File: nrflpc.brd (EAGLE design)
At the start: 67.9 x 38.8 mm, 75 parts, among them IC1 LPC1111/12/13/14-HVQFN33, IC2 LT1763CS8-3.3, IC3 LM3401, IC5 LM3401, IC6 LM3401, IC7 LM3401, Q1 20MHz, Q2 MOSFET-PCHANNEL, Q3 MOSFET-PCHANNEL, Q4 MOSFET-PCHANNEL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

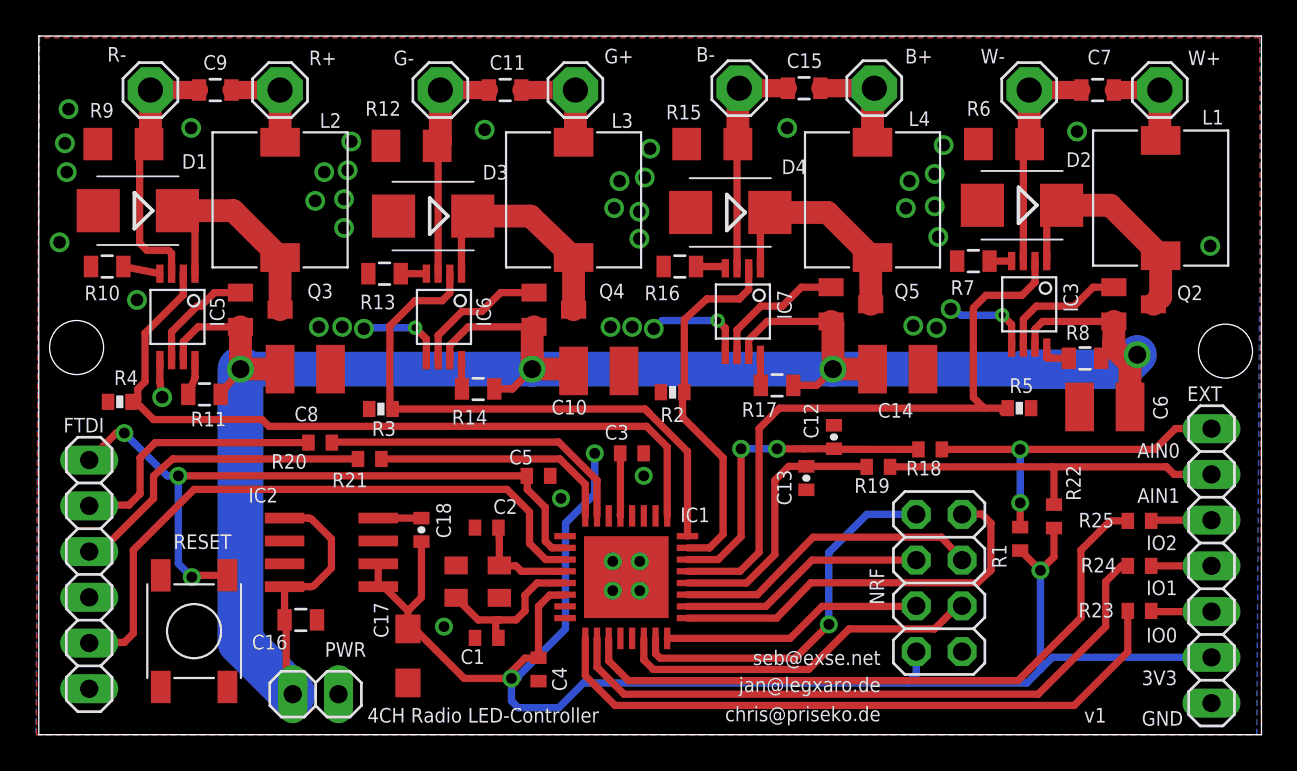
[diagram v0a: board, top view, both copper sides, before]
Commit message: More silkscreen
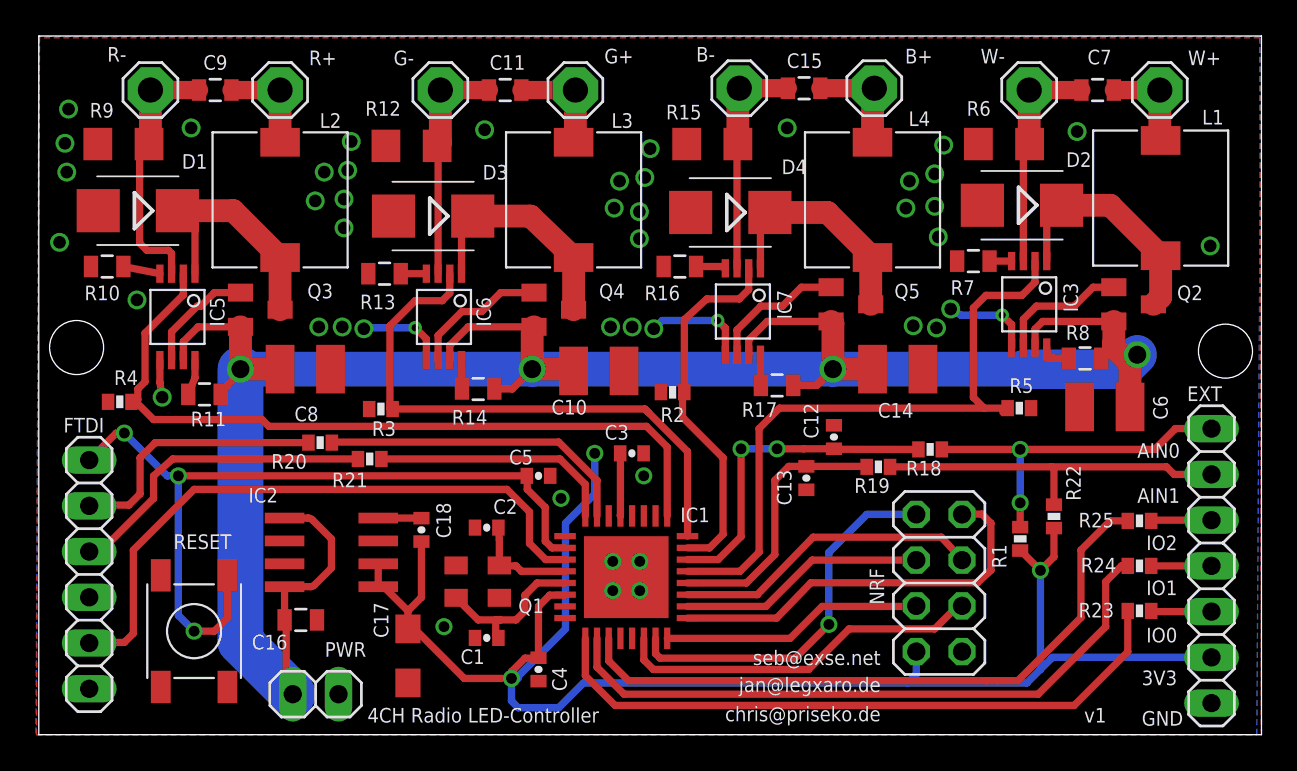
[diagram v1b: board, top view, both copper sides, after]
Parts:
- C1, C2, C3, C4, C5: device rcl:C0402 -> SparkFun-Passives:0402-CAP
- C12, C13: device SparkFun:0402-CAP -> SparkFun-Passives:0402-CAP
- R1, R18, R19, R20, R21, R22, R23, R24, R25: device rcl:R0402 -> SparkFun-Resistors:0402-RES
- R2, R3, R4, R5: device SparkFun:0402-RES -> SparkFun-Resistors:0402-RES
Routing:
- net !RST: track 39.2 -> 44.7 mm
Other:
- board text added: "Q1"

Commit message: Silkscreen
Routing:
- net GND: vias 48 -> 60
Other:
- board text added: "<<</>>"
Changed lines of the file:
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@@
 <grid distance="0.125" unitdist="mm" unit="mm" style="dots" multiple="1" display="yes" altdistance="0.03125" altunitdist="mm" altunit="mm"/>
 <layers>
-<layer number="1" name="Top" color="4" fill="1" visible="yes" active="yes"/>
+<layer number="1" name="Top" color="4" fill="1" visible="no" active="yes"/>
 <layer number="2" name="Route2" color="1" fill="3" visible="no" active="no"/>
 <layer number="3" name="Route3" color="4" fill="3" visible="no" active="no"/>
@@
 <layer number="14" name="Route14" color="1" fill="6" visible="no" active="no"/>
 <layer number="15" name="Route15" color="4" fill="6" visible="no" active="no"/>
-<layer number="16" name="Bottom" color="1" fill="1" visible="yes" active="yes"/>
+<layer number="16" name="Bottom" color="1" fill="1" visible="no" active="yes"/>
 <layer number="17" name="Pads" color="2" fill="1" visible="yes" active="yes"/>
 <layer number="18" name="Vias" color="2" fill="1" visible="yes" active="yes"/>
 <layer number="19" name="Unrouted" color="6" fill="1" visible="yes" active="yes"/>
 <layer number="20" name="Dimension" color="15" fill="1" visible="yes" active="yes"/>
-<layer number="21" name="tPlace" color="15" fill="1" visible="no" active="yes"/>
+<layer number="21" name="tPlace" color="15" fill="1" visible="yes" active="yes"/>
 <layer number="22" name="bPlace" color="7" fill="1" visible="no" active="yes"/>
 <layer number="23" name="tOrigins" color="15" fill="1" visible="yes" active="yes"/>
-<layer number="24" name="bOrigins" color="15" fill="1" visible="yes" active="yes"/>
+<layer number="24" name="bOrigins" color="15" fill="1" visible="no" active="yes"/>
 <layer number="25" name="tNames" color="10" fill="1" visible="yes" active="yes"/>
-<layer number="26" name="bNames" color="7" fill="1" visible="no" active="yes"/>
+<layer number="26" name="bNames" color="7" fill="1" visible="yes" active="yes"/>
 <layer number="27" name="tValues" color="7" fill="1" visible="no" active="yes"/>
-<layer number="28" name="bValues" color="7" fill="1" visible="yes" active="yes"/>
+<layer number="28" name="bValues" color="7" fill="1" visible="no" active="yes"/>
 <layer number="29" name="tStop" color="12" fill="1" visible="yes" active="yes"/>
 <layer number="30" name="bStop" color="7" fill="6" visible="no" active="yes"/>
 <layer number="31" name="tCream" color="7" fill="4" visible="no" active="yes"/>
-<layer number="32" name="bCream" color="7" fill="5" visible="yes" active="yes"/>
+<layer number="32" name="bCream" color="7" fill="5" visible="no" active="yes"/>
 <layer number="33" name="tFinish" color="6" fill="3" visible="no" active="yes"/>
-<layer number="34" name="bFinish" color="6" fill="6" visible="yes" active="yes"/>
+<layer number="34" name="bFinish" color="6" fill="6" visible="no" active="yes"/>
 <layer number="35" name="tGlue" color="7" fill="4" visible="no" active="yes"/>
-<layer number="36" name="bGlue" color="7" fill="5" visible="yes" active="yes"/>
+<layer number="36" name="bGlue" color="7" fill="5" visible="no" active="yes"/>
 <layer number="37" name="tTest" color="7" fill="1" visible="no" active="yes"/>
-<layer number="38" name="bTest" color="7" fill="1" visible="yes" active="yes"/>
+<layer number="38" name="bTest" color="7" fill="1" visible="no" active="yes"/>
 <layer number="39" name="tKeepout" color="4" fill="11" visible="no" active="yes"/>
 <layer number="40" name="bKeepout" color="1" fill="11" visible="no" active="yes"/>
@@
 <wire x1="25.95" y1="33.45" x2="28.4" y2="33.45" width="0.127" layer="121"/>
 <wire x1="31" y1="33.45" x2="33.45" y2="33.45" width="0.127" layer="121"/>
-<wire x1="50.05" y1="33.45" x2="50.05" y2="25.95" width="0.127" layer="121"/>
 <wire x1="50.05" y1="25.95" x2="47.6" y2="25.95" width="0.127" layer="121"/>
 <wire x1="45" y1="25.95" x2="42.55" y2="25.95" width="0.127" layer="121"/>
@@
 <text x="61.25" y="0.5" size="0.8128" layer="21" font="vector" ratio="10">GND</text>
 <text x="26.625" y="6.75" size="0.8128" layer="25">Q1</text>
+<text x="65.875" y="31.375" size="6.4516" layer="26" font="fixed" rot="MR0">&lt;&lt;&lt;/&gt;&gt;</text>
 </plain>
 <attributes>
@@
 <via x="8.625" y="5.75" extent="1-16" drill="0.6"/>
 <wire x1="7.75" y1="14.375" x2="7.75" y2="6.625" width="0.4064" layer="16"/>
-<wire x1="10.475" y1="8.85" x2="8.6" y2="8.85" width="0" layer="19" extent="1-16"/>
 <wire x1="7.75" y1="6.625" x2="8.625" y2="5.75" width="0.4064" layer="16"/>
 <wire x1="8.625" y1="5.75" x2="9.75" y2="5.75" width="0.4064" layer="1"/>
@@
 <wire x1="13.65" y1="6.295" x2="13.74" y2="6.295" width="0.4064" layer="1"/>
 <wire x1="13.74" y1="6.295" x2="13.74" y2="2.615" width="0.4064" layer="1"/>
+<wire x1="13.74" y1="2.615" x2="14.105" y2="2.25" width="0.4064" layer="1"/>
 <wire x1="13.65" y1="6.295" x2="13.65" y2="6.375" width="0" layer="19" extent="1-1"/>
-<wire x1="13.74" y1="2.615" x2="14.105" y2="2.25" width="0.4064" layer="1"/>
 </signal>
 <signal name="TXD">
@@
 <via x="29" y="13.125" extent="1-16" drill="0.6"/>
 <contactref element="RESET" pad="2A"/>
+<via x="18.375" y="4.5" extent="1-16" drill="0.6"/>
+<via x="17.25" y="6.375" extent="1-16" drill="0.6"/>
+<via x="22.5" y="2.375" extent="1-16" drill="0.6"/>
+<via x="5.25" y="1.25" extent="1-16" drill="0.6"/>
+<via x="60.25" y="2" extent="1-16" drill="0.6"/>
+<via x="53.875" y="7.75" extent="1-16" drill="0.6"/>
+<via x="53.75" y="5.5" extent="1-16" drill="0.6"/>
+<via x="44.375" y="13.125" extent="1-16" drill="0.6"/>
+<via x="43" y="12.125" extent="1-16" drill="0.6"/>
+<via x="37.875" y="17.75" extent="1-16" drill="0.6"/>
+<via x="52" y="17" extent="1-16" drill="0.6"/>
+<via x="16.625" y="12.5" extent="1-16" drill="0.6"/>
 </signal>
 <signal name="N$1">
